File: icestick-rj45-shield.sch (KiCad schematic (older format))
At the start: 0 parts

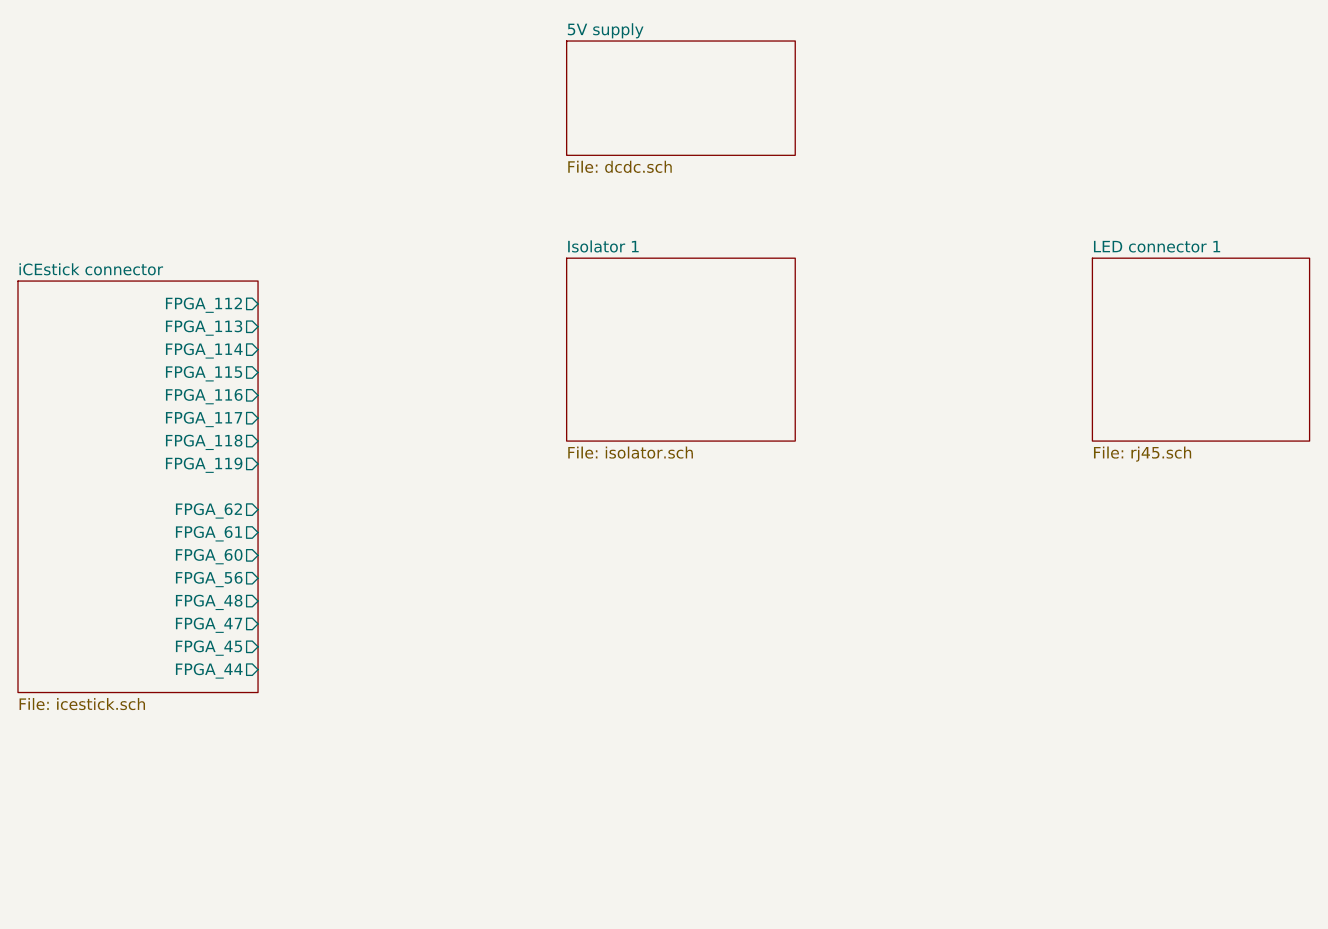
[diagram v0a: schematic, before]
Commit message: Added library for project specific symbols
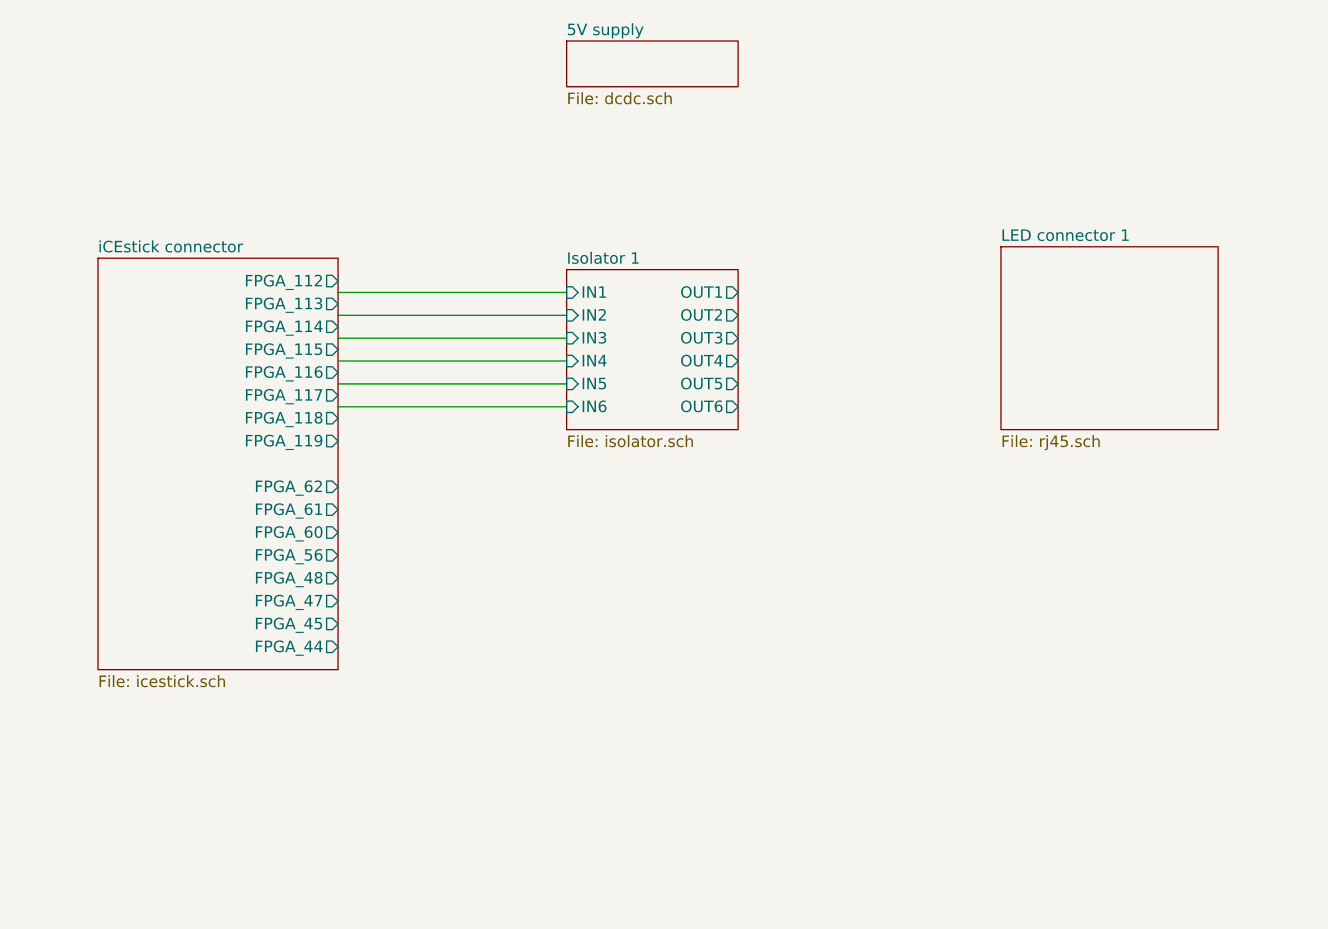
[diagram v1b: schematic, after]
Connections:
- wire segments 0 -> 6
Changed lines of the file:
@@
 $EndDescr
 $Sheet
-S 3400 2500 1050 1800
+S 3750 2400 1050 1800
 U 5BCC5758
 F0 "iCEstick connector" 50
 F1 "icestick.sch" 50
-F2 "FPGA_112" O R 4450 2600 50
-F3 "FPGA_113" O R 4450 2700 50
-F4 "FPGA_114" O R 4450 2800 50
-F5 "FPGA_115" O R 4450 2900 50
-F6 "FPGA_116" O R 4450 3000 50
-F7 "FPGA_117" O R 4450 3100 50
-F8 "FPGA_118" O R 4450 3200 50
-F9 "FPGA_119" O R 4450 3300 50
-F10 "FPGA_62" O R 4450 3500 50
-F11 "FPGA_61" O R 4450 3600 50
-F12 "FPGA_60" O R 4450 3700 50
-F13 "FPGA_56" O R 4450 3800 50
-F14 "FPGA_48" O R 4450 3900 50
-F15 "FPGA_47" O R 4450 4000 50
-F16 "FPGA_45" O R 4450 4100 50
-F17 "FPGA_44" O R 4450 4200 50
+F2 "FPGA_112" O R 4800 2500 50
+F3 "FPGA_113" O R 4800 2600 50
+F4 "FPGA_114" O R 4800 2700 50
+F5 "FPGA_115" O R 4800 2800 50
+F6 "FPGA_116" O R 4800 2900 50
+F7 "FPGA_117" O R 4800 3000 50
+F8 "FPGA_118" O R 4800 3100 50
+F9 "FPGA_119" O R 4800 3200 50
+F10 "FPGA_62" O R 4800 3400 50
+F11 "FPGA_61" O R 4800 3500 50
+F12 "FPGA_60" O R 4800 3600 50
+F13 "FPGA_56" O R 4800 3700 50
+F14 "FPGA_48" O R 4800 3800 50
+F15 "FPGA_47" O R 4800 3900 50
+F16 "FPGA_45" O R 4800 4000 50
+F17 "FPGA_44" O R 4800 4100 50
 $EndSheet
 $Sheet
-S 5800 2400 1000 800
+S 5800 2450 750  700
 U 5BCC578B
 F0 "Isolator 1" 50
 F1 "isolator.sch" 50
+F2 "IN1" I L 5800 2550 50
+F3 "IN2" I L 5800 2650 50
+F4 "OUT1" O R 6550 2550 50
+F5 "OUT2" O R 6550 2650 50
+F6 "OUT3" O R 6550 2750 50
+F7 "OUT4" O R 6550 2850 50
+F8 "OUT5" O R 6550 2950 50
+F9 "OUT6" O R 6550 3050 50
+F10 "IN3" I L 5800 2750 50
+F11 "IN4" I L 5800 2850 50
+F12 "IN5" I L 5800 2950 50
+F13 "IN6" I L 5800 3050 50
 $EndSheet
 $Sheet
-S 5800 1450 1000 500
+S 5800 1450 750  200
 U 5BCC57F6
 F0 "5V supply" 50
@@
 $EndSheet
 $Sheet
-S 8100 2400 950  800
+S 7700 2350 950  800
 U 5BCC584F
 F0 "LED connector 1" 50
 F1 "rj45.sch" 50
 $EndSheet
+Wire Wire Line
+	4800 2550 5800 2550
+Wire Wire Line
+	4800 2650 5800 2650
+Wire Wire Line
+	4800 2750 5800 2750
+Wire Wire Line
+	4800 2850 5800 2850
+Wire Wire Line
+	4800 2950 5800 2950
+Wire Wire Line
+	4800 3050 5800 3050
 $EndSCHEMATC

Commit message: Added isolators and RJ-45 connectors
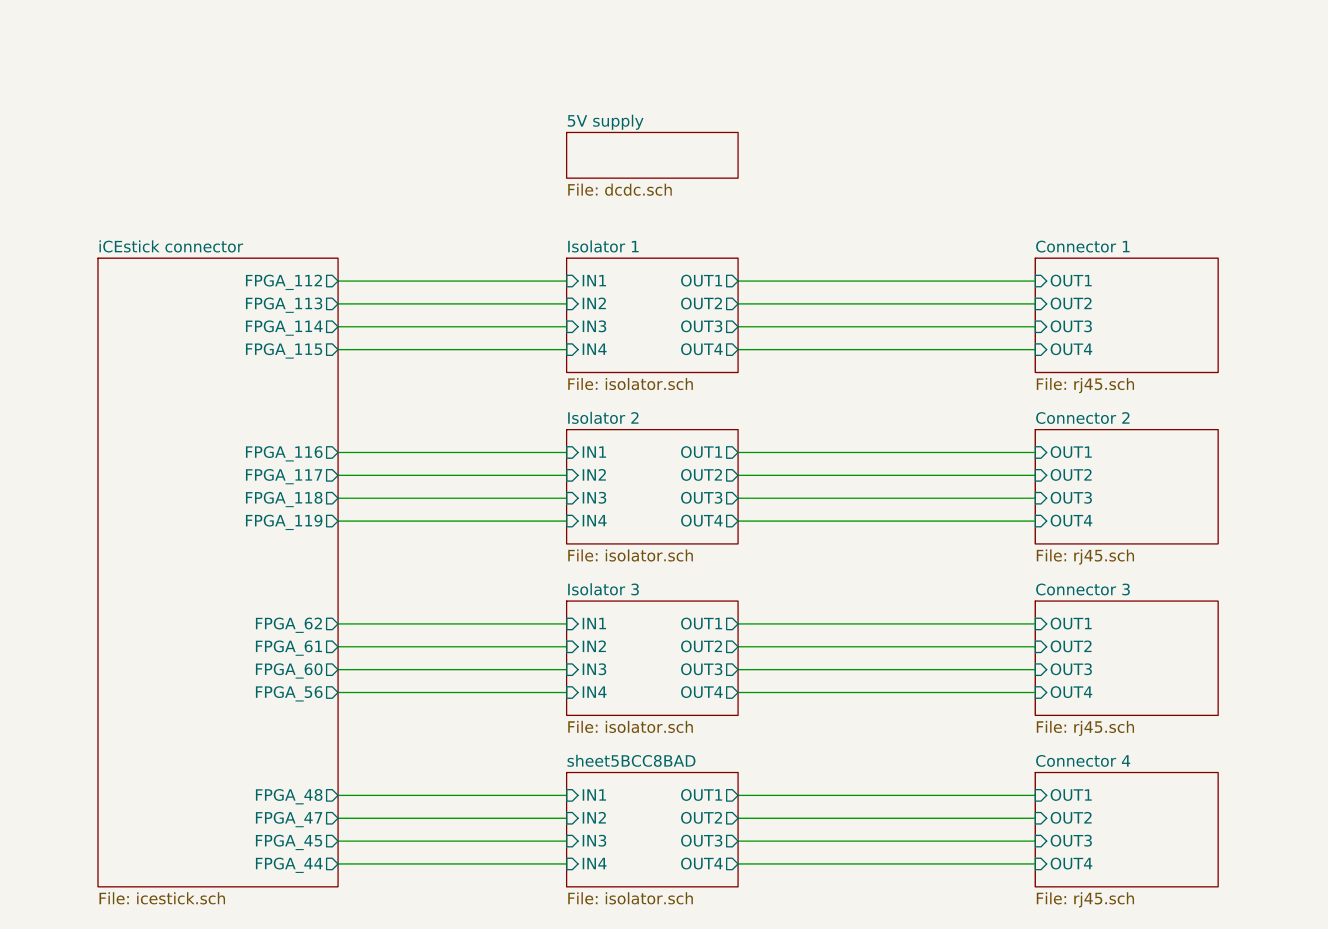
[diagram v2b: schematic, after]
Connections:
- wire segments 6 -> 32
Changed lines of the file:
@@
 $Descr A4 11693 8268
 encoding utf-8
-Sheet 1 5
+Sheet 1 8
 Title ""
 Date ""
@@
 $EndDescr
 $Sheet
-S 3750 2400 1050 1800
+S 3750 2400 1050 2750
 U 5BCC5758
 F0 "iCEstick connector" 50
@@
 F4 "FPGA_114" O R 4800 2700 50
 F5 "FPGA_115" O R 4800 2800 50
-F6 "FPGA_116" O R 4800 2900 50
-F7 "FPGA_117" O R 4800 3000 50
-F8 "FPGA_118" O R 4800 3100 50
-F9 "FPGA_119" O R 4800 3200 50
-F10 "FPGA_62" O R 4800 3400 50
-F11 "FPGA_61" O R 4800 3500 50
-F12 "FPGA_60" O R 4800 3600 50
-F13 "FPGA_56" O R 4800 3700 50
-F14 "FPGA_48" O R 4800 3800 50
-F15 "FPGA_47" O R 4800 3900 50
-F16 "FPGA_45" O R 4800 4000 50
-F17 "FPGA_44" O R 4800 4100 50
-$EndSheet
-$Sheet
-S 5800 2450 750  700
+F6 "FPGA_116" O R 4800 3250 50
+F7 "FPGA_117" O R 4800 3350 50
+F8 "FPGA_118" O R 4800 3450 50
+F9 "FPGA_119" O R 4800 3550 50
+F10 "FPGA_62" O R 4800 4000 50
+F11 "FPGA_61" O R 4800 4100 50
+F12 "FPGA_60" O R 4800 4200 50
+F13 "FPGA_56" O R 4800 4300 50
+F14 "FPGA_48" O R 4800 4750 50
+F15 "FPGA_47" O R 4800 4850 50
+F16 "FPGA_45" O R 4800 4950 50
+F17 "FPGA_44" O R 4800 5050 50
+$EndSheet
+$Sheet
+S 5800 2400 750  500
 U 5BCC578B
 F0 "Isolator 1" 50
 F1 "isolator.sch" 50
-F2 "IN1" I L 5800 2550 50
-F3 "IN2" I L 5800 2650 50
-F4 "OUT1" O R 6550 2550 50
-F5 "OUT2" O R 6550 2650 50
-F6 "OUT3" O R 6550 2750 50
-F7 "OUT4" O R 6550 2850 50
-F8 "OUT5" O R 6550 2950 50
-F9 "OUT6" O R 6550 3050 50
-F10 "IN3" I L 5800 2750 50
-F11 "IN4" I L 5800 2850 50
-F12 "IN5" I L 5800 2950 50
-F13 "IN6" I L 5800 3050 50
-$EndSheet
-$Sheet
-S 5800 1450 750  200
+F2 "IN1" I L 5800 2500 50
+F3 "IN2" I L 5800 2600 50
+F4 "OUT1" O R 6550 2500 50
+F5 "OUT2" O R 6550 2600 50
+F6 "OUT3" O R 6550 2700 50
+F7 "OUT4" O R 6550 2800 50
+F8 "IN3" I L 5800 2700 50
+F9 "IN4" I L 5800 2800 50
+$EndSheet
+$Sheet
+S 5800 1850 750  200
 U 5BCC57F6
 F0 "5V supply" 50
 F1 "dcdc.sch" 50
 $EndSheet
-$Sheet
-S 7700 2350 950  800
-U 5BCC584F
-F0 "LED connector 1" 50
-F1 "rj45.sch" 50
-$EndSheet
-Wire Wire Line
-	4800 2550 5800 2550
-Wire Wire Line
-	4800 2650 5800 2650
-Wire Wire Line
-	4800 2750 5800 2750
-Wire Wire Line
-	4800 2850 5800 2850
-Wire Wire Line
-	4800 2950 5800 2950
-Wire Wire Line
-	4800 3050 5800 3050
+Wire Wire Line
+	4800 2500 5800 2500
+Wire Wire Line
+	4800 2600 5800 2600
+Wire Wire Line
+	4800 2700 5800 2700
+Wire Wire Line
+	4800 2800 5800 2800
+$Sheet
+S 5800 3900 750  500
+U 5BCC7A96
+F0 "Isolator 3" 50
+F1 "isolator.sch" 50
+F2 "IN1" I L 5800 4000 50
+F3 "IN2" I L 5800 4100 50
+F4 "OUT1" O R 6550 4000 50
+F5 "OUT2" O R 6550 4100 50
+F6 "OUT3" O R 6550 4200 50
+F7 "OUT4" O R 6550 4300 50
+F8 "IN3" I L 5800 4200 50
+F9 "IN4" I L 5800 4300 50
+$EndSheet
+$Sheet
+S 5800 3150 750  500
+U 5BCC79AE
+F0 "Isolator 2" 50
+F1 "isolator.sch" 50
+F2 "IN1" I L 5800 3250 50
+F3 "IN2" I L 5800 3350 50
+F4 "OUT1" O R 6550 3250 50
+F5 "OUT2" O R 6550 3350 50
+F6 "OUT3" O R 6550 3450 50
+F7 "OUT4" O R 6550 3550 50
+F8 "IN3" I L 5800 3450 50
+F9 "IN4" I L 5800 3550 50
+$EndSheet
+$Sheet
+S 5800 4650 750  500
+U 5BCC8BB7
+F0 "sheet5BCC8BAD" 50
+F1 "isolator.sch" 50
+F2 "IN1" I L 5800 4750 50
+F3 "IN2" I L 5800 4850 50
+F4 "OUT1" O R 6550 4750 50
+F5 "OUT2" O R 6550 4850 50
+F6 "OUT3" O R 6550 4950 50
+F7 "OUT4" O R 6550 5050 50
+F8 "IN3" I L 5800 4950 50
+F9 "IN4" I L 5800 5050 50
+$EndSheet
+Wire Wire Line
+	5800 3250 4800 3250
+Wire Wire Line
+	4800 3350 5800 3350
+Wire Wire Line
+	4800 3450 5800 3450
+Wire Wire Line
+	4800 3550 5800 3550
+Wire Wire Line
+	4800 4000 5800 4000
+Wire Wire Line
+	4800 4100 5800 4100
+Wire Wire Line
+	4800 4200 5800 4200
+Wire Wire Line
+	4800 4300 5800 4300
+Wire Wire Line
+	4800 4750 5800 4750
+Wire Wire Line
+	4800 4850 5800 4850
+Wire Wire Line
+	4800 4950 5800 4950
+Wire Wire Line
+	4800 5050 5800 5050
+$Sheet
+S 7850 2400 800  500
+U 5BCCA241
+F0 "Connector 1" 50
+F1 "rj45.sch" 50
+F2 "OUT1" I L 7850 2500 50
+F3 "OUT2" I L 7850 2600 50
+F4 "OUT3" I L 7850 2700 50
+F5 "OUT4" I L 7850 2800 50
+$EndSheet
+Wire Wire Line
+	7850 2800 6550 2800
+Wire Wire Line
+	6550 2700 7850 2700
+Wire Wire Line
+	7850 2600 6550 2600
+Wire Wire Line
+	6550 2500 7850 2500
+$Sheet
+S 7850 3150 800  500
+U 5BCCB065
+F0 "Connector 2" 50
+F1 "rj45.sch" 50
+F2 "OUT1" I L 7850 3250 50
+F3 "OUT2" I L 7850 3350 50
+F4 "OUT3" I L 7850 3450 50
+F5 "OUT4" I L 7850 3550 50
+$EndSheet
+Wire Wire Line
+	7850 3550 6550 3550
+Wire Wire Line
+	6550 3450 7850 3450
+Wire Wire Line
+	7850 3350 6550 3350
+Wire Wire Line
+	6550 3250 7850 3250
+$Sheet
+S 7850 3900 800  500
+U 5BCCB3D0
+F0 "Connector 3" 50
+F1 "rj45.sch" 50
+F2 "OUT1" I L 7850 4000 50
+F3 "OUT2" I L 7850 4100 50
+F4 "OUT3" I L 7850 4200 50
+F5 "OUT4" I L 7850 4300 50
+$EndSheet
+Wire Wire Line
+	7850 4300 6550 4300
+Wire Wire Line
+	6550 4200 7850 4200
+Wire Wire Line
+	7850 4100 6550 4100
+Wire Wire Line
+	6550 4000 7850 4000
+$Sheet
+S 7850 4650 800  500
+U 5BCCB87F
+F0 "Connector 4" 50
+F1 "rj45.sch" 50
+F2 "OUT1" I L 7850 4750 50
+F3 "OUT2" I L 7850 4850 50
+F4 "OUT3" I L 7850 4950 50
+F5 "OUT4" I L 7850 5050 50
+$EndSheet
+Wire Wire Line
+	7850 5050 6550 5050
+Wire Wire Line
+	6550 4950 7850 4950
+Wire Wire Line
+	7850 4850 6550 4850
+Wire Wire Line
+	6550 4750 7850 4750
 $EndSCHEMATC
